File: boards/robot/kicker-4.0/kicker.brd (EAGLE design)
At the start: 141 x 146.1 mm, 158 parts, among them J4 SFW8R-1STE1LF, J5 436500217, J6 436500202, J7 436500202, J8 430450411, Q1 BSS127, Q100 AOD1N60, Q101 BSS127, Q2 BSS127, Q3 BSS127, Q4 BSS806NSOT-23-3, Q6 IXGK400N30A3, Q7 IXGK400N30A3, Q8 IRFS4227, T1 DA203X-ALDA2034, U1 IX4427N, U100 15V, U2 MPM3620GQV-P, U3 ADUM7441CRQZ-RL7, U4 ADUM7441ARQZ-RL7, U5 AT32ATQFP44, U6 LT3751FE

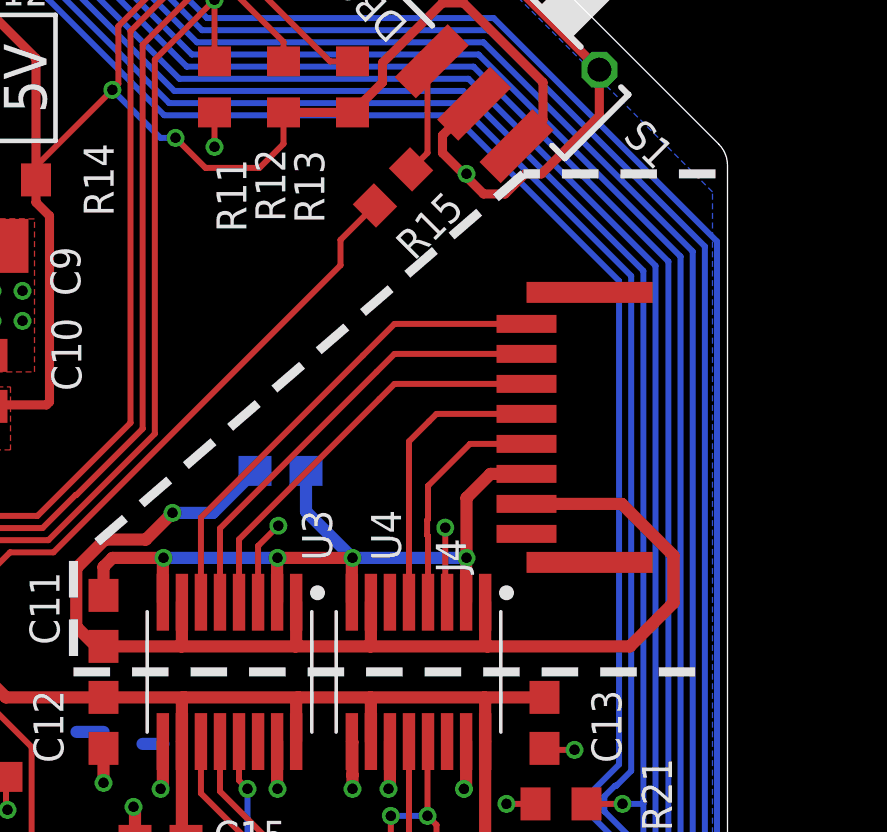
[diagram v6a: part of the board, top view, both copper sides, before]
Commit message: Changed SFW8R-1STE1LF for SFW8S-2STE1LF
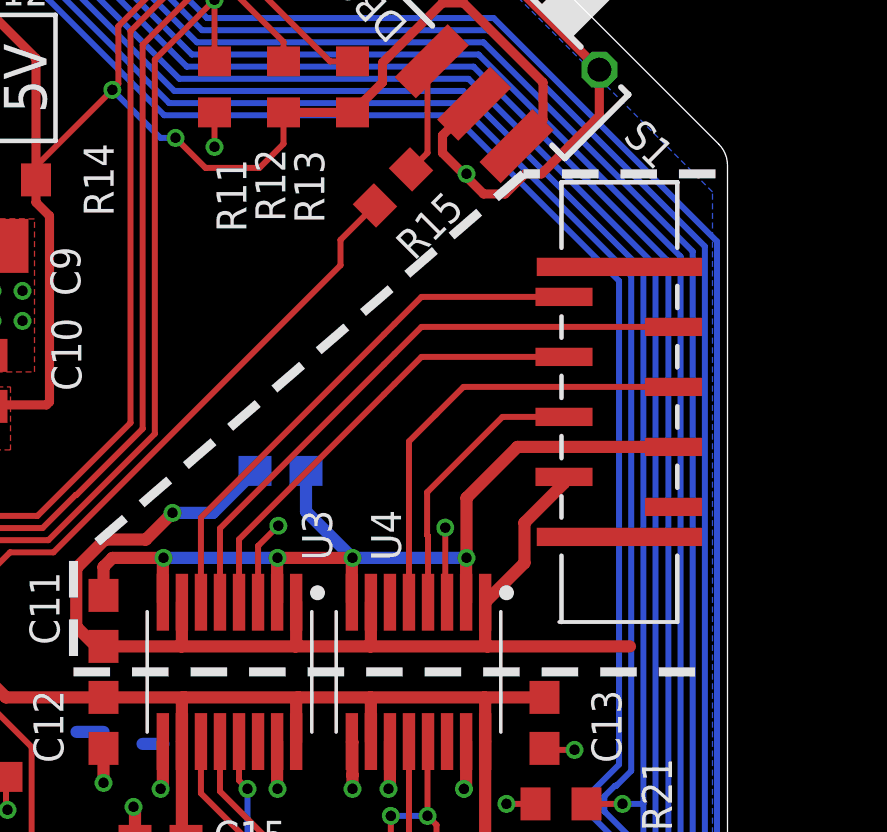
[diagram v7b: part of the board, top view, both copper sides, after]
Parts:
- removed J4: SFW8R-1STE1LF, RoboJackets-Connectors:SFW8R-1STE1LF
- added J1: SFW8S-2STE1LF, RoboJackets-Connectors:CON8_1X8_UB_SFW_JAE
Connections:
- net !KICKER_SELECT_EXT: now also J1.5; no longer J4.P$6
- net !RESET_EXT: now also J1.4; no longer J4.P$5
- net GND_LGC_EXT: now also J1.3; no longer J4.P$4
- net MISO_EXT: now also J1.8; no longer J4.P$9
- net MOSI_EXT: now also J1.7; no longer J4.P$8
- net SCK_EXT: now also J1.6; no longer J4.P$7
- net VCC_LGC_EXT: now also J1.2; no longer J4.P$3
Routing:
- net GND_LGC_EXT: track 27.0 -> 32.3 mm
- net MOSI_EXT: track 15.1 -> 20.4 mm
- net !KICKER_SELECT_EXT: track 9.66 -> 14.9 mm
- net VCC_LGC_EXT: track 43.2 -> 39.2 mm
- net SCK_EXT: track 13.8 -> 15.4 mm
- net MISO_EXT: track 16.4 -> 18.0 mm
- net !RESET_EXT: track 7.77 -> 9.28 mm
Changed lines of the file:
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@@
 <attribute name="SPICEPREFIX" value="C" x="57.4" y="-21.64" size="1" layer="27" font="vector" rot="R270" display="off"/>
-</element>
-<element name="J4" library="RoboJackets-Connectors" package="SFW8R-1STE1LF" value="SFW8R-1STE1LF" x="68" y="33" smashed="yes" rot="R90">
-<attribute name="NAME" x="61.778" y="33" size="1" layer="25" font="vector" rot="R90"/>
 </element>
 <element name="R103" library="RoboJackets-Resistors" package="TO508P1539X450-3" value="1.0k 3.5W" x="11.3" y="48.2" smashed="yes" rot="MR180">
@@
 <attribute name="MPN" value="LTST-C191KGKT" x="-34" y="67" size="1" layer="27" font="vector" rot="R90" display="off"/>
 <attribute name="NAME" x="-31" y="72" size="1" layer="25" font="vector" rot="R180"/>
+</element>
+<element name="J1" library="RoboJackets-Connectors" package="CON8_1X8_UB_SFW_JAE" value="SFW8S-2STE1LF" x="68.7" y="35.2" smashed="yes" rot="R90">
+<attribute name="NAME" x="63.255" y="36.4286" size="1.27" layer="27" ratio="6" rot="SR90"/>
 </element>
 </elements>
@@
 <wire x1="58.6125" y1="32.0215" x2="58.6125" y2="30.5625" width="0.4064" layer="1"/>
 <wire x1="58.6125" y1="30.5625" x2="58.6" y2="30.55" width="0.4064" layer="1"/>
-<contactref element="J4" pad="P$3"/>
 <wire x1="62.5" y1="30.55" x2="58.6" y2="30.55" width="0.4064" layer="1"/>
 <wire x1="62.4225" y1="32.0215" x2="62.4225" y2="30.6275" width="0.4064" layer="1"/>
 <wire x1="62.4225" y1="30.6275" x2="62.5" y2="30.55" width="0.4064" layer="1"/>
-<wire x1="63.8" y1="35.3" x2="66.97728125" y2="35.3" width="0.4064" layer="1"/>
-<wire x1="66.97728125" y1="35.3" x2="68.7" y2="33.57728125" width="0.4064" layer="1"/>
-<wire x1="68.7" y1="32" x2="68.7" y2="33.57728125" width="0.4064" layer="1"/>
-<wire x1="67.25" y1="30.55" x2="68.7" y2="32" width="0.4064" layer="1"/>
 <wire x1="62.5" y1="30.55" x2="67.25" y2="30.55" width="0.4064" layer="1"/>
 <wire x1="49.7" y1="30.55" x2="49.45" y2="30.55" width="0.4064" layer="1"/>
@@
 <wire x1="54.75" y1="36.4" x2="53.35" y2="35" width="0.4064" layer="16"/>
 <wire x1="53.35" y1="35" x2="52" y2="35" width="0.4064" layer="16"/>
+<contactref element="J1" pad="2"/>
+<wire x1="62.4225" y1="32.0215" x2="63.732503125" y2="33.331503125" width="0.4064" layer="1"/>
+<wire x1="65.05" y1="35.99138125" x2="65.05" y2="36.2" width="0.4064" layer="1"/>
+<wire x1="63.732503125" y1="33.331503125" x2="63.732503125" y2="34.673884375" width="0.4064" layer="1"/>
+<wire x1="63.732503125" y1="34.673884375" x2="65.05" y2="35.99138125" width="0.4064" layer="1"/>
 </signal>
 <signal name="GND_LGC_EXT">
@@
 <wire x1="61.7875" y1="32.0215" x2="61.7875" y2="33.4875" width="0.4064" layer="1"/>
 <wire x1="61.7875" y1="33.4875" x2="61.8" y2="33.5" width="0.4064" layer="1"/>
-<contactref element="J4" pad="P$4"/>
-<wire x1="63.8" y1="36.3" x2="62.6" y2="36.3" width="0.4064" layer="1"/>
-<wire x1="62.6" y1="36.3" x2="61.8" y2="35.5" width="0.4064" layer="1"/>
-<wire x1="61.8" y1="35.5" x2="61.8" y2="33.5" width="0.4064" layer="1"/>
+<wire x1="61.8" y1="33.5" x2="61.8" y2="35.5" width="0.4064" layer="1"/>
 <wire x1="58" y1="33.5" x2="56.45" y2="35.05" width="0.4064" layer="16"/>
 <wire x1="56.45" y1="35.05" x2="56.45" y2="36.4" width="0.4064" layer="16"/>
+<contactref element="J1" pad="3"/>
+<wire x1="63.5" y1="37.2" x2="68.7" y2="37.2" width="0.4064" layer="1"/>
+<wire x1="61.8" y1="35.5" x2="63.5" y2="37.2" width="0.4064" layer="1"/>
 </signal>
 <signal name="!RESET_EXT">
 <contactref element="U4" pad="4"/>
-<contactref element="J4" pad="P$5"/>
-<wire x1="63.8" y1="37.3" x2="61.9175" y2="37.3" width="0.2" layer="1"/>
-<wire x1="61.9175" y1="37.3" x2="60.5175" y2="35.9" width="0.2" layer="1"/>
+<contactref element="J1" pad="4"/>
+<wire x1="63" y1="38.200003125" x2="65.05" y2="38.200003125" width="0.2" layer="1"/>
 <wire x1="60.5175" y1="32.0215" x2="60.5175" y2="34.2269" width="0.2" layer="1"/>
 <wire x1="60.5175" y1="34.2269" x2="60.4868" y2="34.2576" width="0.2" layer="1"/>
-<wire x1="60.4868" y1="34.2576" x2="60.4868" y2="34.7588" width="0.2" layer="1"/>
-<wire x1="60.4868" y1="34.7588" x2="60.5175" y2="34.7895" width="0.2" layer="1"/>
-<wire x1="60.5175" y1="34.7895" x2="60.5175" y2="35.9" width="0.2" layer="1"/>
+<wire x1="60.4868" y1="34.2576" x2="60.4868" y2="35.686803125" width="0.2" layer="1"/>
+<wire x1="60.4868" y1="35.686803125" x2="63" y2="38.200003125" width="0.2" layer="1"/>
 </signal>
 <signal name="!KICKER_SELECT_EXT">
 <contactref element="U4" pad="5"/>
-<wire x1="59.8825" y1="37.3825" x2="60.55" y2="38.05" width="0.2" layer="1"/>
+<wire x1="59.8825" y1="37.3825" x2="60.75" y2="38.25" width="0.2" layer="1"/>
+<wire x1="60.75" y1="38.25" x2="60.8" y2="38.3" width="0.2" layer="1"/>
 <wire x1="59.8825" y1="32.0215" x2="59.8825" y2="37.3825" width="0.2" layer="1"/>
-<contactref element="J4" pad="P$6"/>
-<wire x1="63.8" y1="38.3" x2="60.8" y2="38.3" width="0.2" layer="1"/>
-<wire x1="60.8" y1="38.3" x2="60.55" y2="38.05" width="0.2" layer="1"/>
+<contactref element="J1" pad="5"/>
+<wire x1="60.8" y1="38.3" x2="61.7" y2="39.2" width="0.2" layer="1"/>
+<wire x1="61.7" y1="39.2" x2="68.7" y2="39.2" width="0.2" layer="1"/>
 </signal>
 <signal name="SCK_EXT">
 <contactref element="U3" pad="4"/>
 <wire x1="54.2175" y1="34.1175" x2="54.2175" y2="32.0215" width="0.2" layer="1"/>
-<contactref element="J4" pad="P$7"/>
-<wire x1="58.9" y1="38.8" x2="54.2175" y2="34.1175" width="0.2" layer="1"/>
-<wire x1="63.8" y1="39.3" x2="59.4" y2="39.3" width="0.2" layer="1"/>
-<wire x1="59.4" y1="39.3" x2="58.9" y2="38.8" width="0.2" layer="1"/>
+<wire x1="59.4" y1="39.3" x2="59.05" y2="38.95" width="0.2" layer="1"/>
+<contactref element="J1" pad="6"/>
+<wire x1="59.05" y1="38.95" x2="54.2175" y2="34.1175" width="0.2" layer="1"/>
+<wire x1="59.4" y1="39.3" x2="60.3" y2="40.2" width="0.2" layer="1"/>
+<wire x1="60.3" y1="40.2" x2="65.05" y2="40.2" width="0.2" layer="1"/>
 </signal>
 <signal name="MOSI_EXT">
 <contactref element="U3" pad="5"/>
 <wire x1="53.5825" y1="34.4825" x2="53.5825" y2="32.0215" width="0.2" layer="1"/>
-<contactref element="J4" pad="P$8"/>
-<wire x1="58.8" y1="39.7" x2="53.5825" y2="34.4825" width="0.2" layer="1"/>
-<wire x1="63.8" y1="40.3" x2="59.4" y2="40.3" width="0.2" layer="1"/>
-<wire x1="59.4" y1="40.3" x2="58.8" y2="39.7" width="0.2" layer="1"/>
+<wire x1="59.4" y1="40.3" x2="59.05" y2="39.95" width="0.2" layer="1"/>
+<contactref element="J1" pad="7"/>
+<wire x1="59.05" y1="39.95" x2="53.5825" y2="34.4825" width="0.2" layer="1"/>
+<wire x1="59.4" y1="40.3" x2="60.3" y2="41.2" width="0.2" layer="1"/>
+<wire x1="60.3" y1="41.2" x2="68.7" y2="41.2" width="0.2" layer="1"/>
 </signal>
 <signal name="MISO_EXT">
 <contactref element="U3" pad="6"/>
 <wire x1="52.9475" y1="34.8475" x2="52.9475" y2="32.0215" width="0.2" layer="1"/>
-<contactref element="J4" pad="P$9"/>
-<wire x1="58.35" y1="40.25" x2="52.9475" y2="34.8475" width="0.2" layer="1"/>
-<wire x1="63.8" y1="41.3" x2="59.4" y2="41.3" width="0.2" layer="1"/>
-<wire x1="59.4" y1="41.3" x2="58.35" y2="40.25" width="0.2" layer="1"/>
+<wire x1="59.4" y1="41.3" x2="59.05" y2="40.95" width="0.2" layer="1"/>
+<contactref element="J1" pad="8"/>
+<wire x1="59.05" y1="40.95" x2="52.9475" y2="34.8475" width="0.2" layer="1"/>
+<wire x1="59.4" y1="41.3" x2="60.3" y2="42.2" width="0.2" layer="1"/>
+<wire x1="60.3" y1="42.2" x2="65.05" y2="42.2" width="0.2" layer="1"/>
 </signal>
 <signal name="MCU_ERR_CL">

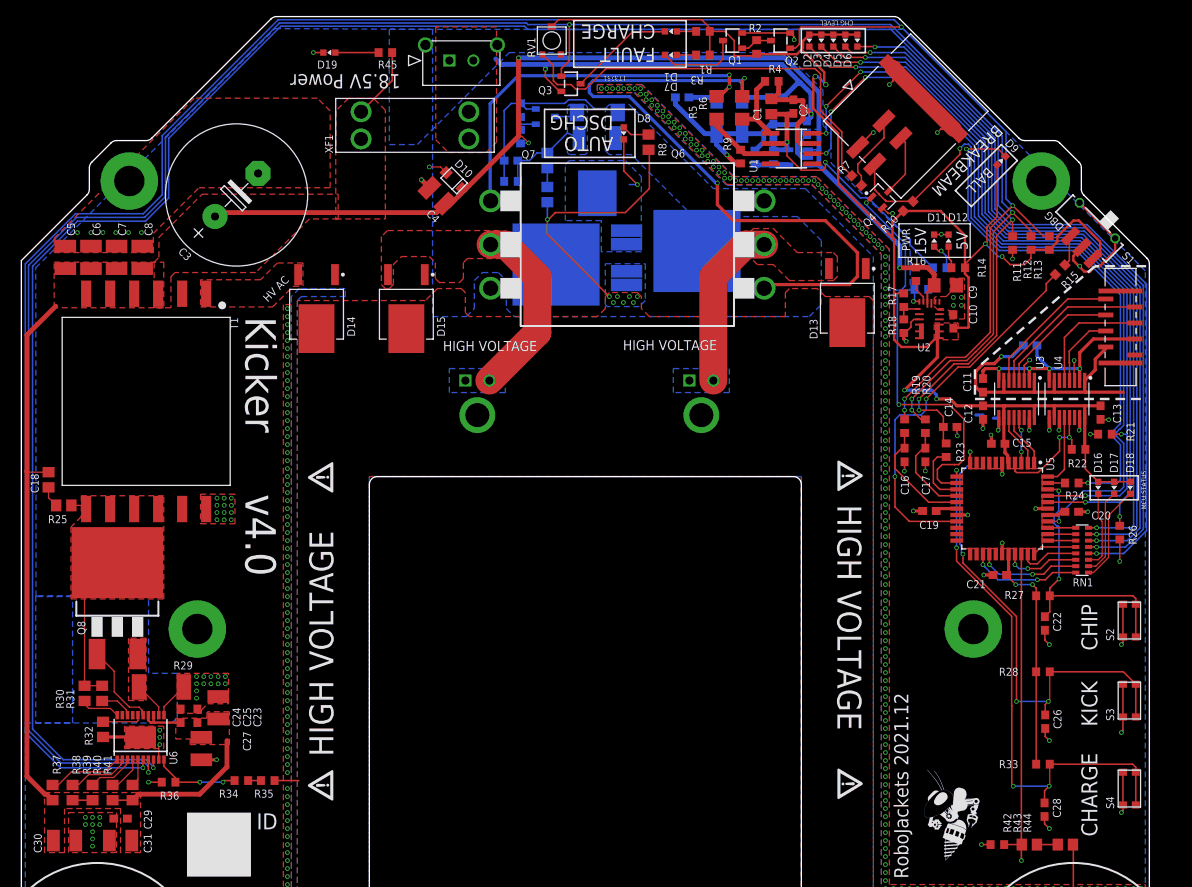
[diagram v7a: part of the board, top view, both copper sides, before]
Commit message: Silkscreen fixes
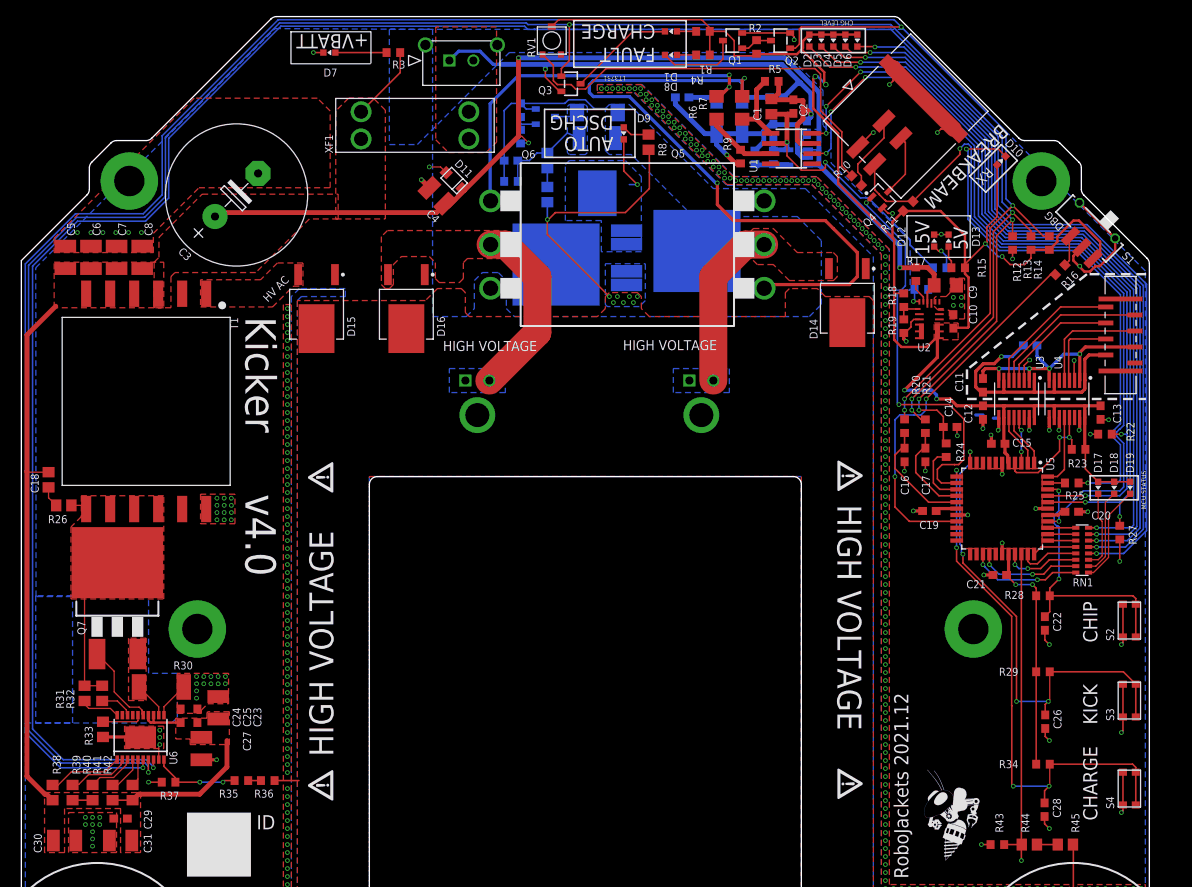
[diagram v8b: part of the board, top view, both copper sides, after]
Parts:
- removed J6: 436500202, RoboJackets-Connectors:CON_436500202_MOL
- removed Q100: AOD1N60, RoboJackets-Discrete:DPAK
- added J3: SFW8S-2STE1LF, RoboJackets-Connectors:CON8_1X8_UB_SFW_JAE
- added Q5: IXGK400N30A3, RoboJackets-Discrete:TO264
- D10: value PTVS20VS1UR -> BLUE; device RoboJackets-Diodes:SOD123-W -> RoboJackets-LEDs:CHIP-LED0603
- D11: value GREEN -> PTVS20VS1UR; device RoboJackets-LEDs:CHIP-LED0603 -> RoboJackets-Diodes:SOD123-W
- D13: value VS-5EWH06FN-M3 -> GREEN; device RoboJackets-Diodes:TO460P990X239-3 -> RoboJackets-LEDs:CHIP-LED0603
- D16: value GREEN -> VS-5EWH06FN-M3; device RoboJackets-LEDs:CHIP-LED0603 -> RoboJackets-Diodes:TO460P990X239-3
- D17: value YELLOW -> GREEN
- D18: value RED -> YELLOW
- D19: value GREEN -> RED
- D7: value RED -> GREEN
- D8: value YELLOW -> RED
- D9: value BLUE -> YELLOW
- J1: value SFW8S-2STE1LF -> 436500217; device RoboJackets-Connectors:CON8_1X8_UB_SFW_JAE -> RoboJackets-Connectors:CON_436500217_MOL
- J5: value 436500217 -> 436500202; device RoboJackets-Connectors:CON_436500217_MOL -> RoboJackets-Connectors:CON_436500202_MOL
- Q7: value IXGK400N30A3 -> IRFS4227; device RoboJackets-Discrete:TO264 -> RoboJackets-Discrete:D2PAK
- Q8: value IRFS4227 -> AOD1N60; device RoboJackets-Discrete:D2PAK -> RoboJackets-Discrete:DPAK
- R10: value 10k -> 51
- R14: value 330 -> 10k
- R15, R4: value 10k -> 330
- R16: value 100k -> 10k
- R17: value 160k 1% -> 100k
- R18: value 30.1k 1% -> 160k 1%
- R19: value 1k -> 30.1k 1%
- R21: value 10k -> 1k
- R23: value 1k -> 10k
- R24: value 160 -> 1k
- R25: value 22 -> 160; device rcl:R0805 -> rcl:R0603
- R26: value 10k -> 22; device rcl:R0603 -> rcl:R0805
- R29: value 10m 0.1% >1W -> 10k; device rcl:R2512 -> rcl:R0603
- R3: value 330 -> 1k
- R30: value 11.5k 0.1% -> 10m 0.1% >1W; device rcl:R0805 -> rcl:R2512
- R31: value 25.5k 0.1% -> 11.5k 0.1%
- R32: value 1k 0.1% -> 25.5k 0.1%
- R33: value 10k -> 1k 0.1%; device rcl:R0603 -> rcl:R0805
- R34: value 114k 0.1% -> 10k
- R35: value 505k 0.1% -> 114k 0.1%
- R36: value 3.12k 0.1% -> 505k 0.1%
- R37: value 25.5k 1% -> 3.12k 0.1%; device rcl:R0805 -> rcl:R0603
- R38: value 294k 1% -> 25.5k 1%
- R39, R41: value 412k 1% -> 294k 1%
- R40: value 294k 1% -> 412k 1%
- R42: value RC0603FR-07102KL -> 412k 1%; device rcl:R0603 -> rcl:R0805
- R43: value ERJ-6GEYJ515V -> RC0603FR-07102KL; device rcl:R0805 -> rcl:R0603
- R45: value 1k -> ERJ-6GEYJ515V; device rcl:R0603 -> rcl:R0805
- R5: value 1k -> 10k; device rcl:R1206 -> rcl:R0603
- R7: value 51 -> 1k; device rcl:R0603 -> rcl:R1206
- moved R26 132.0 mm to (-65.2, 16.4), turned to 180 degrees
- moved R45 130.5 mm to (60.0, -26.0)
- moved R25 126.0 mm to (60.8, 19.2)
- moved R33 117.6 mm to (-60.3, -11.6), turned to 270 degrees
- moved D19 113.9 mm to (68.1, 18.6), turned to 180 degrees
- moved R29 110.2 mm to (57.2, -4.40)
- moved R42 108.3 mm to (-56.6, -19.5), turned to 90 degrees
- moved R34 100.2 mm to (57.2, -15.9)
- moved J1 93.3 mm to (-17.0, 72.0), turned to 180 degrees
- moved D16 89.3 mm to (-22.4, 41.0), turned to 270 degrees
- moved Q7 85.7 mm to (-58.5, 6.70), turned to 0 degrees
- moved Q8 78.3 mm to (1.50, 57.0), flipped to the bottom, turned to 180 degrees
- moved D10 68.4 mm to (52.0, 59.5), turned to 315 degrees
- moved D14 66.4 mm to (32.8, 41.8)
- moved D11 60.5 mm to (-16.4, 57.0), turned to 135 degrees
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- renumbered C100 to C36, C101 to C37, C102 to C38, C103 to C39, C104 to C40, C105 to C41, D100 to D20, D101 to D21, D102 to D22, J7 to J4, J8 to J2, Q101 to Q9, R100 to R46, R101 to R47, R102 to R48, R103 to R49, R104 to R50, R105 to R51, R106 to R52, R107 to R53, R108 to R54, R109 to R55, R110 to R56, U$100 to U$6, U$101 to U$7, U$102 to U$8, U$103 to U$9, U$104 to U$10, U100 to U7
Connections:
- net !BTN_CHG: now also R34.1; no longer R33.1
- net !BTN_CHP: now also R28.1; no longer R27.1
- net !BTN_KCK: now also R29.1; no longer R28.1
- net !DONE!: now also R21.1; no longer R20.1
- net !DONE!_RAW: now also R13.1, R21.2; no longer R12.1, R20.2
- net !FAULT!: now also R20.1; no longer R19.1
- net !FAULT!_RAW: now also R14.1, R20.2; no longer R13.1, R19.2
- net !KICKER_SELECT_EXT: now also J3.5; no longer J1.5
- net !RESET: now also R23.1; no longer R22.1
- net !RESET_EXT: now also J3.4; no longer J1.4
- net +5V: now also D10.A, D19.A, R11.2, R15.2, R18.2, R23.2, R29.2, R34.2, R4.2; no longer D16.A, D9.A, R10.2, R12.2, R17.2, R22.2, R27.2, R3.2, R33.2
- net 15V_PWR_BR: now also D12.A; no longer D11.A
- net 15V_PWR_BR1: now also D7.A, R3.1; no longer D19.A, R45.1
- net BALL_SENSE: now also R25.2; no longer R24.2
- net BALL_SENSE_CL: now also D10.C, R25.1; no longer D9.C, R24.1
- net BB_RX: now also R11.1; no longer R10.1
- net BB_TX_CL: now also R10.2; no longer R7.2
- net CHARGE: now also R24.1; no longer R23.1
- net CHARGE_RAW: now also R12.2, R24.2; no longer R11.2, R23.2
- net CHIP: now also R22.2; no longer R21.2
- net CHIPPER: now also D16.2, J5.2, Q5.C_BOT; no longer D15.2, J6.2, Q6.C_BOT
- net CHIP_GATE: now also R6.1; no longer R5.1
- net CHIP_GATE_S: now also Q5.G_BOT, R6.2; no longer Q6.G_BOT, R5.2
- net CSP: now also Q7.3, R30.2; no longer Q8.3, R29.2
- net DISCHARGE_DRAIN: now also D9.C, Q8.4; no longer D8.C, Q100.4
- net FB: now also R18.1, R19.2; no longer R17.1, R18.2
- net GND: now also D11.A, D13.C, D7.C, J1.1, Q5.E_BOT, Q8.3, R12.1, R19.1, R22.1, R27.1, R30.1, R33.2, R37.2, R43.1, R5.1; no longer D10.A, D11.C, D19.C, J5.1, Q100.3, Q7.E_BOT, R11.1, R18.1, R21.1, R26.1, R29.1, R32.2, R36.2, R4.1, R42.1
- net GND_LGC_EXT: now also J3.3; no longer J1.3
- net HVGATE: now also Q7.1; no longer Q8.1
- net HV_AC: now also D15.2; no longer D14.2
- net HV_FB: now also R35.2, R37.1; no longer R34.2, R36.1
- net HV_SENSE_DIV_BR: now also R44.2, R45.1; no longer R43.2, R44.1
- net KICK: now also R27.2; no longer R26.2
- net KICKER: now also D14.2, Q6.C_BOT; no longer D13.2, Q7.C_BOT
- net KICK_GATE: now also R5.2, R7.1; no longer R4.2, R6.1
- net KICK_GATE_S: now also Q6.G_BOT, R7.2; no longer Q7.G_BOT, R6.2
- net MCU_ERR_CL: now also D19.C; no longer D18.C
- net MCU_INIT_OK_CL: now also D17.C; no longer D16.C
- net MCU_MODE_CL: now also D18.C; no longer D17.C
- net MISO_EXT: now also J3.8; no longer J1.8
- net MODE_SELECT: now also R16.2; no longer R15.2
- net MOSI_EXT: now also J3.7; no longer J1.7
- net N$1: now also R33.1; no longer R32.1
- net N$14: now also R16.1; no longer R15.1
- net N$18: now also R26.2; no longer R25.2
- net N$2: now also R35.1, R36.2; no longer R34.1, R35.2
- net N$20: now also D13.A, R15.1; no longer D12.A, R14.1
- net N$24: now also R38.1; no longer R37.1
- net N$27: now also D8.A, R4.1; no longer D7.A, R3.1
- net N$28: now also D8.C; no longer D7.C
- net N$29: now also D9.A; no longer D8.A
- net N$3: now also R10.1; no longer R7.1
- net N$39: now also J1.2; no longer J5.2
- net OVLO1: now also R40.2; no longer R39.2
- net OVLO2: now also R42.2; no longer R41.2
- net QUICK_DISCHARGE: now also Q8.1; no longer Q100.1
- net RDCM: now also R31.2; no longer R30.2
- net REG_EN: now also R17.2; no longer R16.2
- net RVOUT: now also R32.2; no longer R31.2
- net SCK_EXT: now also J3.6; no longer J1.6
- net UVLO1: now also R39.2; no longer R38.2
- net UVLO2: now also R41.2; no longer R40.2
- net V+: now also D16.3, J5.1, R36.1, R45.2; no longer D13.3, J6.1, R35.1, R44.2
- net VBATT: now also D11.C, R17.1, R3.2, R38.2, R42.1; no longer D10.C, R16.1, R37.2, R38.1, R45.2
- net VCC_LGC_EXT: now also J3.2; no longer J1.2
- net VMON: now also R43.2, R44.1; no longer R42.2, R43.1
- net VSN: now also Q7.2, R26.1, R32.1; no longer Q8.2, R25.1, R30.1
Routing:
- net GND: track 252.8 -> 259.5 mm
- net VCC_LGC_EXT: track 39.2 -> 34.3 mm
- net !FAULT!_RAW: track 287.1 -> 285.7 mm
- net !DONE!_RAW: track 276.0 -> 274.8 mm
- net CHARGE_RAW: track 269.0 -> 268.0 mm
- net 15V_PWR_BR1: track 5.40 -> 6.40 mm
- net !KICKER_SELECT_EXT: track 14.9 -> 14.4 mm
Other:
- board text added: "+VBATT"
- board text added: "RX"
- board text removed: "18.5V Power"
- board text removed: "BALL"
- board text removed: "PWR"
